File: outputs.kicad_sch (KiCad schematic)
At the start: 11 parts, among them J10 Screw_Terminal_01x03, J11 Screw_Terminal_01x03, U2 74AHCT1G125, U3 74AHCT1G125

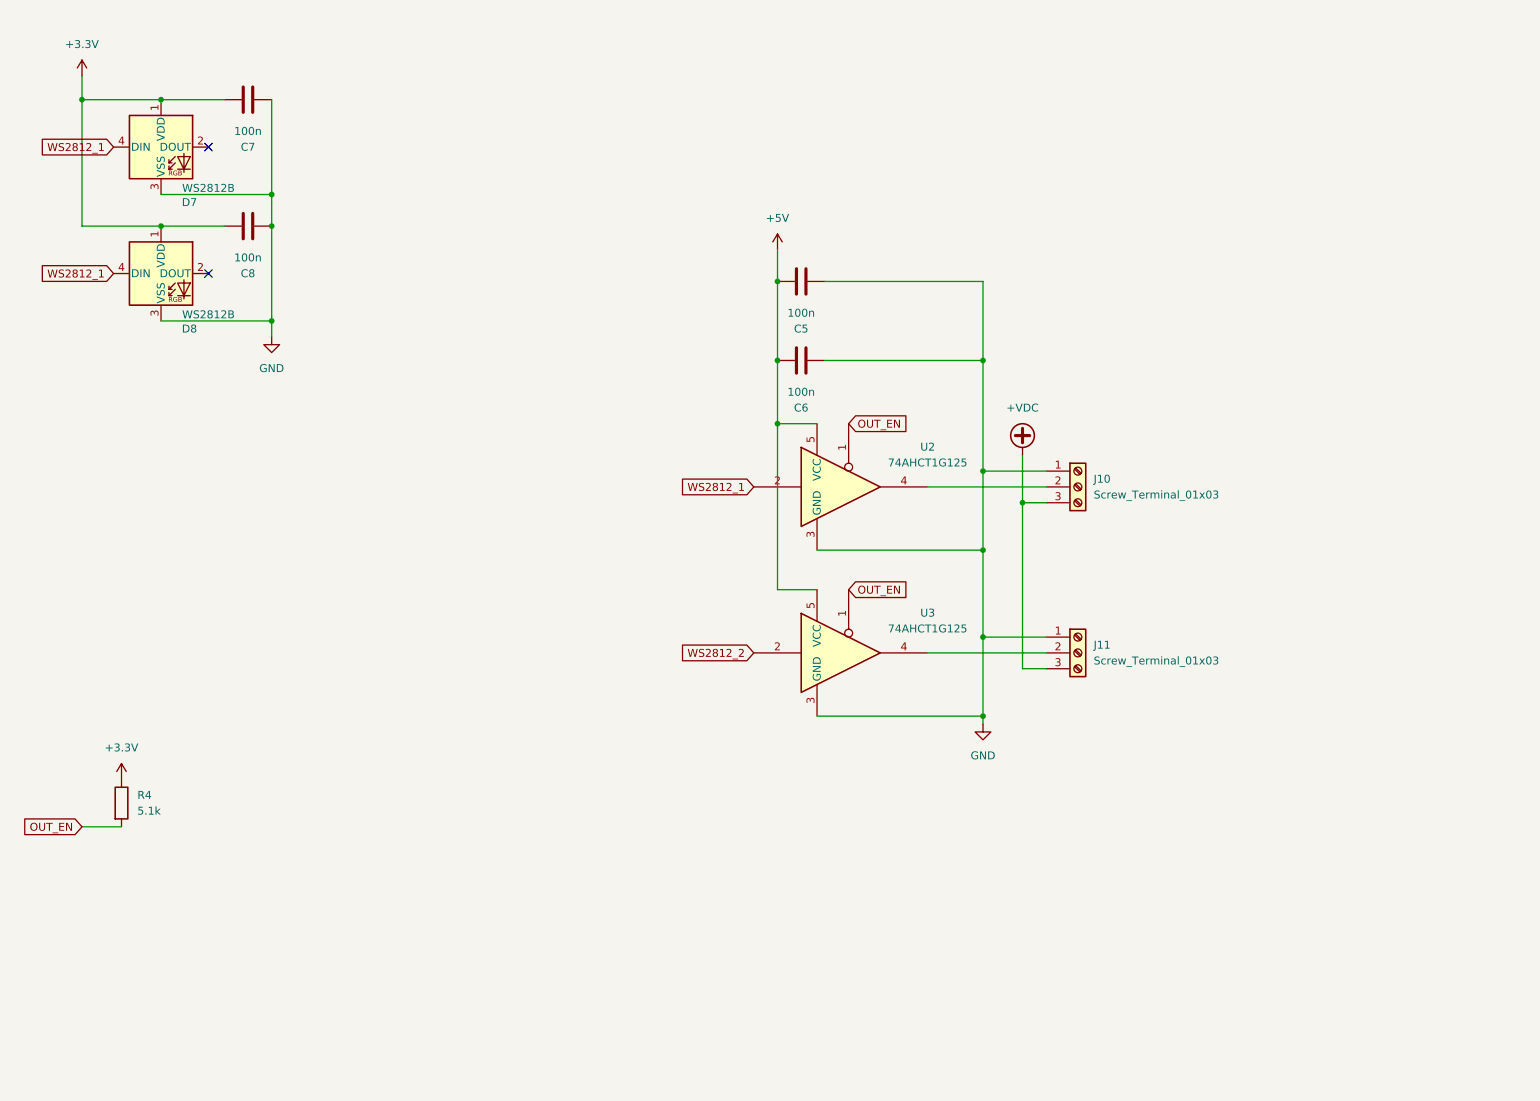
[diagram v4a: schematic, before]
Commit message: complete top layer layout
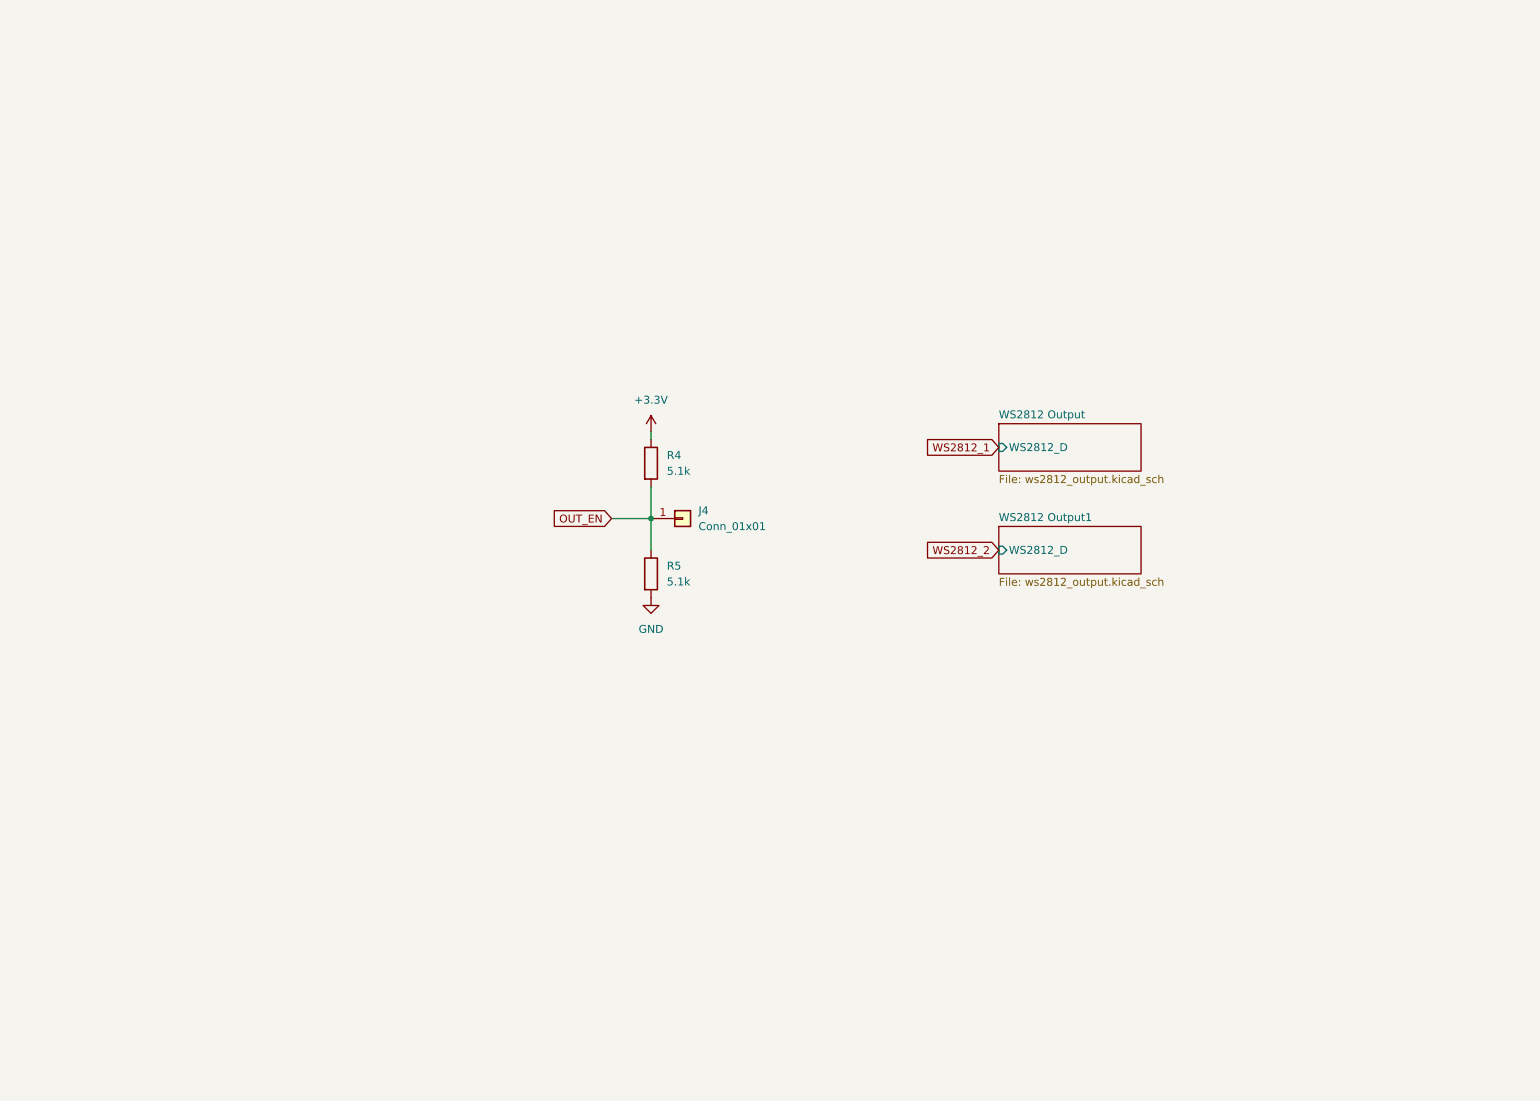
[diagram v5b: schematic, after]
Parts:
- removed C5, C6, C7, C8: 100n, Capacitor_SMD:C_0603_1608Metric_Pad1.08x0.95mm_HandSolder, symbol Device:C
- removed D7, D8: WS2812B, LED_SMD:LED_WS2812B_PLCC4_5.0x5.0mm_P3.2mm, symbol LED:WS2812B
- removed J10, J11: Screw_Terminal_01x03, TerminalBlock_MetzConnect:TerminalBlock_MetzConnect_Type101_RT01603HBWC_1x03_P5.08mm_Horizontal, symbol Connector:Screw_Terminal_01x03
- removed U2, U3: 74AHCT1G125, Package_TO_SOT_SMD:SOT-353_SC-70-5_Handsoldering, symbol 74xGxx:74AHCT1G125
- added J4: Conn_01x01, Connector_PinHeader_2.54mm:PinHeader_1x01_P2.54mm_Vertical, symbol Connector_Generic:Conn_01x01
- added R5: 5.1k, Resistor_SMD:R_0603_1608Metric_Pad0.98x0.95mm_HandSolder, symbol Device:R
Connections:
- net GND: now also R5.2
- net OUT_EN: now also J4.1 (Pin_1), R5.1
- no-connect marks 2 -> 0
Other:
- added sheet WS2812 Output (ws2812_output.kicad_sch)
- added sheet WS2812 Output1 (ws2812_output.kicad_sch)
- moved on the sheet: R4
